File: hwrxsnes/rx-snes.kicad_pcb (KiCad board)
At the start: 2 copper layers, 28.4 x 18.7 mm, 20 parts, among them IC1 ATMEGA328-A, P1 +5v, P2 Clock, P3 Latch, P4 Data, P5 GND, P6 nRF, P7 ISP, P8 RX, P9 TX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

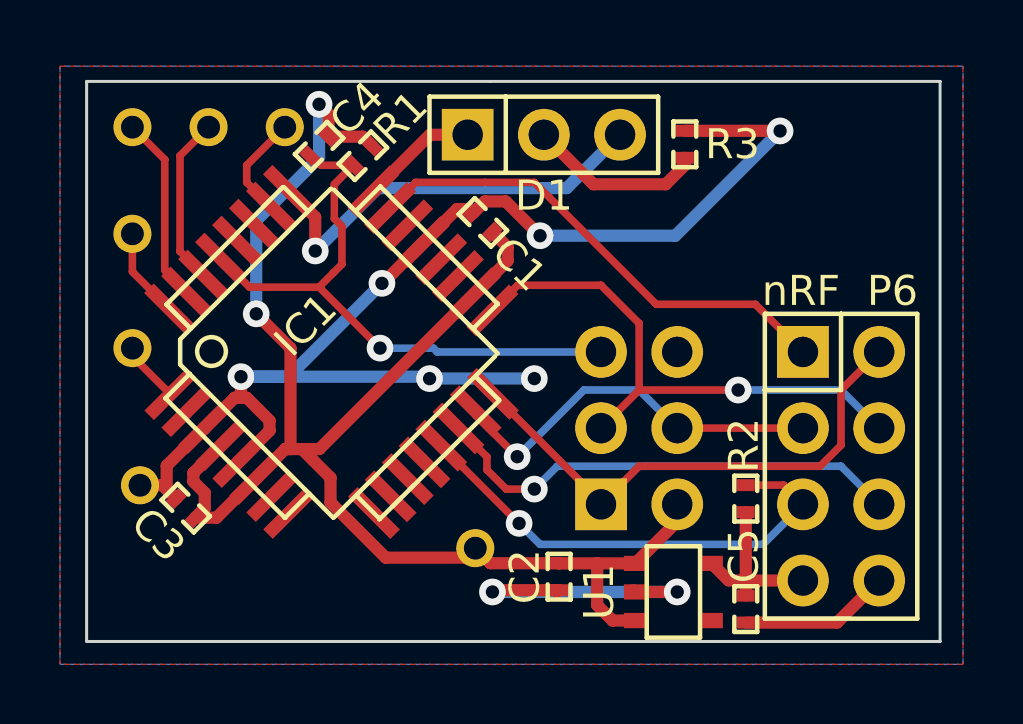
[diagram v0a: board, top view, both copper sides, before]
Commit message: Reroute the SNES RX board.
Both to add a 16MHz crystal and align the holes for easier wiring.

Refs #2
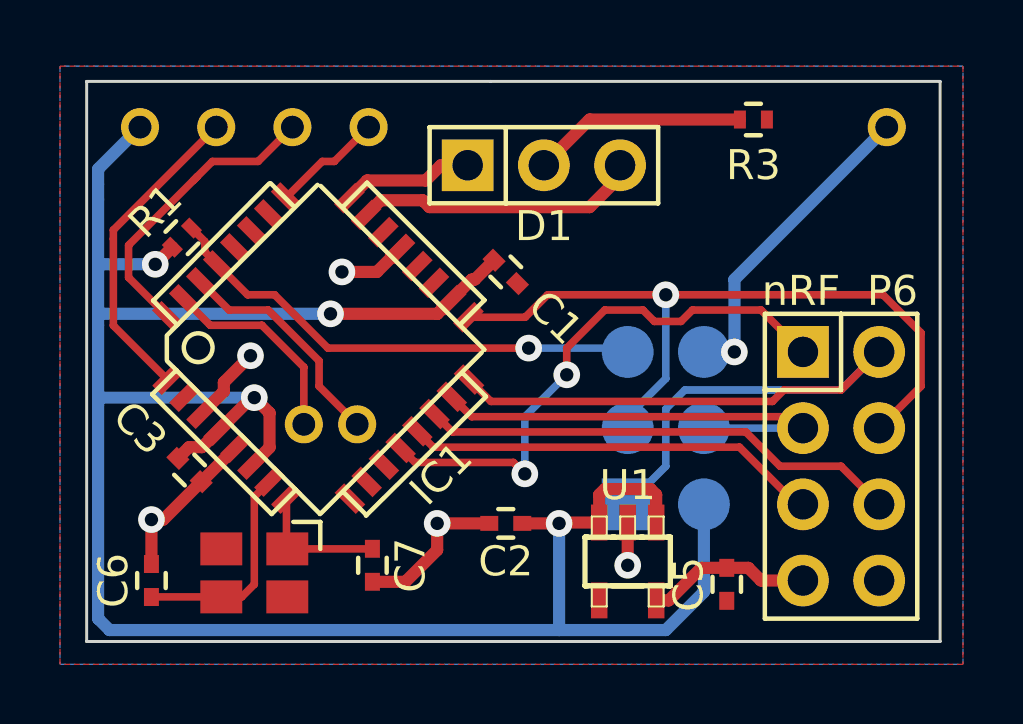
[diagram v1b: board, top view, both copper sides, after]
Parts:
- removed C4: 0.1u, SMD_Packages:SMD-0402_c
- removed R2: 10k, SMD_Packages:SMD-0402_r
- added C6: 22p, Capacitors_SMD:C_0402, F.Cu at (27.6, 42.0)
- added C7: 22p, Capacitors_SMD:C_0402, F.Cu at (34.9, 41.5)
- added X1: CRYSTAL, nesRF:TSX-3225, F.Cu at (31.0, 41.8)
- C1, C2, C3, C5: footprint SMD_Packages:SMD-0402_c -> Capacitors_SMD:C_0402
- IC1: footprint SMD_Packages:TQFP-32 -> nesRF:TQFP-32
- P1: value +5v -> +5v (Wht)
- P2: value Clock -> Clock (Yel)
- P3: value Latch -> Latch (Org)
- P4: value Data -> Data (Red)
- P5: value GND -> GND (Brn)
- P7: footprint Pin_Headers:Pin_Header_Straight_2x03 -> nesRF:ISP_POGO
- R1, R3: footprint SMD_Packages:SMD-0402_r -> Resistors_SMD:R_0402
- U1: footprint SMD_Packages:SOT-23-5 -> nesRF:SOT23-5
- moved P5 27.6 mm to (52.1, 26.9), turned to 0 degrees
- moved P1 17.9 mm to (27.2, 26.9)
- moved P9 11.4 mm to (32.6, 36.8)
- moved P8 11.1 mm to (34.4, 36.8)
- moved P2 7.88 mm to (29.7, 26.9)
- moved R1 6.62 mm to (28.6, 30.6), turned to 225 degrees
- moved P3 6.41 mm to (32.3, 26.9)
- moved P4 2.79 mm to (34.8, 26.9)
- moved C2 2.51 mm to (39.4, 40.1), turned to 0 degrees
- moved R3 2.43 mm to (47.6, 26.7), turned to 0 degrees
- moved U1 1.83 mm to (43.4, 41.4), turned to 180 degrees
- moved C1 1.82 mm to (39.4, 31.8), turned to 315 degrees
- moved C3 1.28 mm to (28.8, 38.4), turned to 315 degrees
- moved C5 1.04 mm to (46.7, 42.2)
- moved D1 1.02 mm to (40.6, 28.2)
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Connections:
- D1 pad 1: /Green -> /Yellow
- D1 pad 3: /Yellow -> /Green
- IC1 pad 12: (no net) -> /RF_IRQ
- IC1 pad 23: /RF_IRQ -> /Green
- IC1 pad 24: /Green -> /Yellow
- IC1 pad 25: /Yellow -> /Data
- IC1 pad 26: /Data -> (no net)
- IC1 pad 7: (no net) -> /XTAL1
- IC1 pad 8: (no net) -> /XTAL2
- R3 pad 1: GND -> /LEDCommon
- R3 pad 2: /LEDCommon -> GND
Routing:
- net GND: track 60.0 -> 26.4 mm, vias 8 -> 6
- net +5V: track 52.8 -> 79.4 mm, vias 2 -> 4
- net /Yellow: track 14.1 -> 4.40 mm, vias 1 -> 0
- net /MISO: track 17.6 -> 26.3 mm
- net /Clock: track 2.06 -> 10.6 mm
- net /XTAL1: track 0.00 -> 7.24 mm
- net /Latch: track 3.04 -> 10.2 mm
- net /SCK: track 18.3 -> 24.6 mm
- net /Green: track 3.93 -> 9.56 mm
- net /XTAL2: track 0.00 -> 4.53 mm
- net /~RST: track 20.2 -> 16.5 mm
- net /MOSI: track 13.1 -> 15.4 mm, vias 1 -> 0
- net /RF_CSN: track 16.1 -> 13.9 mm, vias 1 -> 0
- net /RF_IRQ: track 16.5 -> 18.6 mm, vias 0 -> 2
- net /SER_RX: track 5.67 -> 7.65 mm
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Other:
- rule trace_min: 0.254 -> 0.01
- rule via_min_size: 0.889 -> 0.035
- board text added: "arantius.com April 2015"
- board text added: "nesRF SNES Receiver"
- board text removed: "Brown"
- board text removed: "ISP"
- board text removed: "Orange"
- board text removed: "Red"
- board text removed: "White"
- board text removed: "Yellow"
- board text removed: "nesRF SNES Receiver arantius.com Jan 2015"
